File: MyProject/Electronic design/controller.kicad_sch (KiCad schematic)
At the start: 2 parts

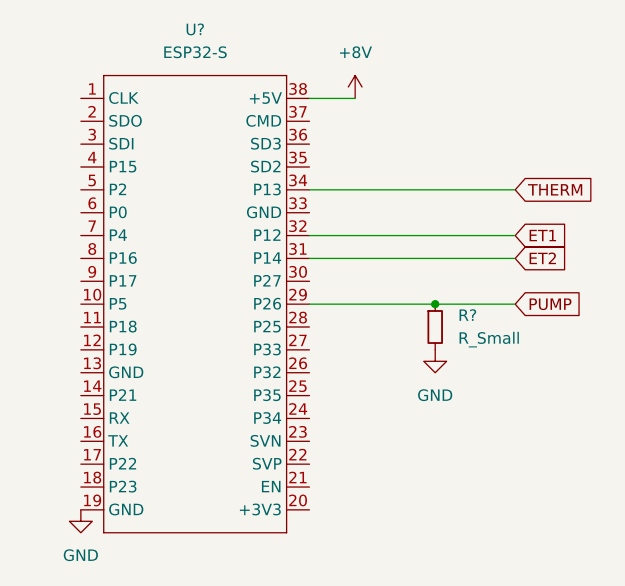
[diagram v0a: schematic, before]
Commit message: Shortening file names for Windows users
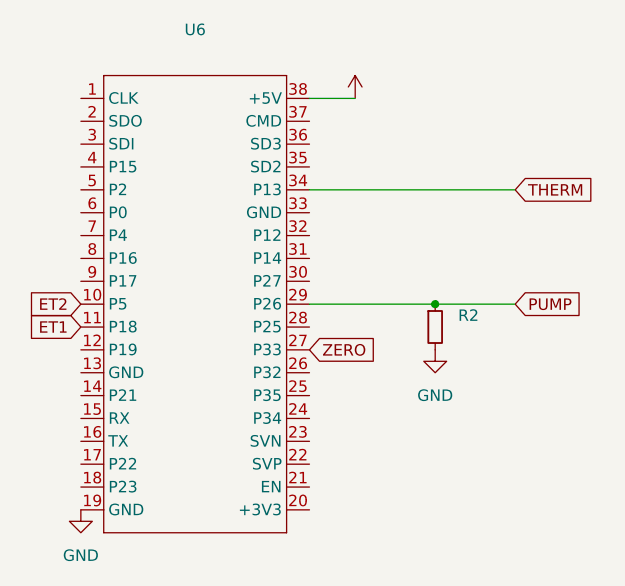
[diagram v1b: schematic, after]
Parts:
- R2: renamed from R?; value R_Small -> (none)
- U6: renamed from U?; value ESP32-S -> (none)
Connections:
- net ET1: now also U6.11 (P18); no longer U6.32 (P12)
- net ET2: now also U6.10 (P5); no longer U6.31 (P14)
- net ZERO: now reaches U6.27 (P33)
- net +8V renamed +5V
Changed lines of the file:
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@@
-    (stroke (width 0) (type default) (color 0 0 0 0))
-  )
-  (wire (pts (xy 157.48 67.31) (xy 134.62 67.31))
     (stroke (width 0) (type default) (color 0 0 0 0))
   )
@@
     (stroke (width 0) (type default) (color 0 0 0 0))
   )
-  (wire (pts (xy 157.48 69.85) (xy 134.62 69.85))
-    (stroke (width 0) (type default) (color 0 0 0 0))
+  (global_label "ET2" (shape input) (at 109.22 74.93 180) (fields_autoplaced)
+    (effects (font (size 1.27 1.27)) (justify right))
+    (property "Intersheet References" "${INTERSHEET_REFS}" (id 0) (at 103.4807 75.0094 0)
+      (effects (font (size 1.27 1.27)) (justify right) hide)
+    )
   )
-  (global_label "ET2" (shape input) (at 157.48 69.85 0) (fields_autoplaced)
+  (global_label "ZERO" (shape input) (at 134.62 80.01 0) (fields_autoplaced)
     (effects (font (size 1.27 1.27)) (justify left))
-    (property "Intersheet References" "${INTERSHEET_REFS}" (id 0) (at 163.2193 69.7706 0)
+    (property "Intersheet References" "${INTERSHEET_REFS}" (id 0) (at 141.9921 80.0894 0)
       (effects (font (size 1.27 1.27)) (justify left) hide)
     )
   )
-  (global_label "ET1" (shape input) (at 157.48 67.31 0) (fields_autoplaced)
-    (effects (font (size 1.27 1.27)) (justify left))
-    (property "Intersheet References" "${INTERSHEET_REFS}" (id 0) (at 163.2193 67.2306 0)
-      (effects (font (size 1.27 1.27)) (justify left) hide)
+  (global_label "ET1" (shape input) (at 109.22 77.47 180) (fields_autoplaced)
+    (effects (font (size 1.27 1.27)) (justify right))
+    (property "Intersheet References" "${INTERSHEET_REFS}" (id 0) (at 103.4807 77.5494 0)
+      (effects (font (size 1.27 1.27)) (justify right) hide)
     )
   )
@@
   (symbol (lib_id "power:GND") (at 148.59 80.01 0) (unit 1)
     (in_bom yes) (on_board yes) (fields_autoplaced)
-    (property "Reference" "#PWR?" (id 0) (at 148.59 86.36 0)
+    (property "Reference" "#PWR0116" (id 0) (at 148.59 86.36 0)
       (effects (font (size 1.27 1.27)) hide)
     )
@@
   (symbol (lib_id "power:GND") (at 109.22 97.79 0) (unit 1)
     (in_bom yes) (on_board yes) (fields_autoplaced)
-    (property "Reference" "#PWR?" (id 0) (at 109.22 104.14 0)
+    (property "Reference" "#PWR0117" (id 0) (at 109.22 104.14 0)
       (effects (font (size 1.27 1.27)) hide)
     )
@@
   (symbol (lib_id "Device:R_Small") (at 148.59 77.47 0) (unit 1)
     (in_bom yes) (on_board yes) (fields_autoplaced)
-    (property "Reference" "R?" (id 0) (at 151.13 76.1999 0)
+    (property "Reference" "R2" (id 0) (at 151.13 76.1999 0)
       (effects (font (size 1.27 1.27)) (justify left))
     )
-    (property "Value" "R_Small" (id 1) (at 151.13 78.7399 0)
+    (property "Value" "" (id 1) (at 151.13 78.7399 0)
       (effects (font (size 1.27 1.27)) (justify left))
     )
@@
     (pin "2")
   )
-  (symbol (lib_id "power:+8V") (at 139.7 52.07 0) (unit 1)
-    (in_bom yes) (on_board yes) (fields_autoplaced)
-    (property "Reference" "#PWR?" (id 0) (at 139.7 55.88 0)
-      (effects (font (size 1.27 1.27)) hide)
-    )
-    (property "Value" "+8V" (id 1) (at 139.7 46.99 0))
-    (property "Footprint" "" (id 2) (at 139.7 52.07 0)
-      (effects (font (size 1.27 1.27)) hide)
-    )
-    (property "Datasheet" "" (id 3) (at 139.7 52.07 0)
-      (effects (font (size 1.27 1.27)) hide)
-    )
-    (pin "1")
-  )
   (symbol (lib_id "Userlibrary:ESP32-S") (at 121.92 74.93 0) (unit 1)
     (in_bom yes) (on_board yes) (fields_autoplaced)
-    (property "Reference" "U?" (id 0) (at 121.92 44.45 0))
-    (property "Value" "ESP32-S" (id 1) (at 121.92 46.99 0))
+    (property "Reference" "U6" (id 0) (at 121.92 44.45 0))
+    (property "Value" "" (id 1) (at 121.92 46.99 0))
     (property "Footprint" "" (id 2) (at 121.92 74.93 0)
       (effects (font (size 1.27 1.27)) hide)
@@
     (pin "9")
   )
+  (symbol (lib_id "power:+5V") (at 139.7 52.07 0) (unit 1)
+    (in_bom yes) (on_board yes) (fields_autoplaced)
+    (property "Reference" "#PWR0115" (id 0) (at 139.7 55.88 0)
+      (effects (font (size 1.27 1.27)) hide)
+    )
+    (property "Value" "" (id 1) (at 139.7 46.99 0))
+    (property "Footprint" "" (id 2) (at 139.7 52.07 0)
+      (effects (font (size 1.27 1.27)) hide)
+    )
+    (property "Datasheet" "" (id 3) (at 139.7 52.07 0)
+      (effects (font (size 1.27 1.27)) hide)
+    )
+    (pin "1")
+  )
 )
